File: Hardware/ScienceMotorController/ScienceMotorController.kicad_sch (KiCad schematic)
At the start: 200 parts

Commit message: Finished schematic and updated footprints
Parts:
- removed D? (x2): YELLOW, LED_SMD:LED_0603_1608Metric_Pad1.05x0.95mm_HandSolder, symbol Device:LED_Small
- removed LimSwitch? (x2): Molex_SL_02, MRDT_Connectors:MOLEX_SL_02_Vertical, symbol MRDT_Connectors:Molex_SL_02
- removed R? (x2): 120, Resistor_SMD:R_0603_1608Metric_Pad0.98x0.95mm_HandSolder, symbol Device:R
- removed Servo? (x2): Molex_SL_03, MRDT_Connectors:MOLEX_SL_03_Vertical, symbol MRDT_Connectors:Molex_SL_03
- added AbsEncode?: Molex_SL_03, MRDT_Connectors:MOLEX_SL_03_Vertical, symbol MRDT_Connectors:Molex_SL_03
- added Conn6: Molex_SL_02, MRDT_Connectors:MOLEX_SL_02_Vertical, symbol MRDT_Connectors:Molex_SL_02
- added D16: LED(B), LED_SMD:LED_0603_1608Metric_Pad1.05x0.95mm_HandSolder, symbol Device:LED
- added D?: YELLOW, LED_SMD:LED_0603_1608Metric_Pad1.05x0.95mm_HandSolder, symbol Device:LED_Small
- added Q10: AO3401A, Package_TO_SOT_SMD:SOT-23, symbol Transistor_FET:AO3401A
- added Q9: BSS138, Package_TO_SOT_SMD:SOT-23, symbol Transistor_FET:BSS138
- added R36: 4.7k, Resistor_SMD:R_0603_1608Metric_Pad0.98x0.95mm_HandSolder, symbol Device:R
- added R37, R38: 10k, Resistor_SMD:R_0603_1608Metric_Pad0.98x0.95mm_HandSolder, symbol Device:R
- added R39: 1k, Resistor_SMD:R_0603_1608Metric_Pad0.98x0.95mm_HandSolder, symbol Device:R
- added R?: 120, Resistor_SMD:R_0603_1608Metric_Pad0.98x0.95mm_HandSolder, symbol Device:R
- R1, R2, R34, R35, R40, R41, R54, R55: renamed from R?; footprint (none) -> Resistor_SMD:R_0603_1608Metric_Pad0.98x0.95mm_HandSolder
- gave numbers to parts that had none: 173
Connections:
- net +12V: now also Q10.2 (S), R37.1
- net +5V: now also AbsEncode?.3
- net Encoder_PWM_4: now also AbsEncode?.2, R?.1
- net FWD_PWM_4: now also U12.6 (OUT1D)
- net GND: now also AbsEncode?.1, Conn6.2, D16.1 (K), D?.1 (K), Q9.2 (S), R36.2
- net RVS_PWM_4: now also U12.7 (RX2)
- net Peristaltic Pump: now reaches U12.28 (RX7)
- net Peristaltic Pump: now also Q9.1 (G), R36.1
- new net: D16.2 (A), R39.1
- new net: Q9.3 (D), R38.2
- new net: Q10.1 (G), R37.2, R38.1
- new net: Conn6.1, Q10.3 (D), R39.2
- new net: D?.2 (A), R?.2
- no-connect marks 14 -> 13
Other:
- note added: "Motor Controllers"
- note removed: "Motor Drivers"
- moved on the sheet: AbsEncode1, AbsEncode2, AbsEncode3, AbsEncode4, C10, C11, C12, C7, C8, C9, Conn7A, Conn7B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

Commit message: Layout generated and organized. Still need to draw traces
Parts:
- added D33: YELLOW, LED_SMD:LED_0603_1608Metric_Pad1.05x0.95mm_HandSolder, symbol Device:LED_Small
- added DY13: LED, LED_SMD:LED_0603_1608Metric_Pad1.05x0.95mm_HandSolder, symbol Device:LED
- added LimSwitch3: Molex_SL_02, MRDT_Connectors:MOLEX_SL_02_Vertical, symbol MRDT_Connectors:Molex_SL_02
- added R58: 100, Resistor_SMD:R_0603_1608Metric_Pad0.98x0.95mm_HandSolder, symbol Device:R
- added R65: 120, Resistor_SMD:R_0603_1608Metric_Pad0.98x0.95mm_HandSolder, symbol Device:R
- added SW12: SW_Push, Button_Switch_SMD:SW_SPST_EVPBF, symbol Switch:SW_Push
- gave numbers to parts that had none: 3
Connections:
- net +3V3: now also LimSwitch3.1, SW12.1
- net GND: now also D33.1 (K), DY13.1 (K)
- net Limit_Switch_8: now also U12.30 (CRX3), LimSwitch3.2, R65.2
- net Motor_5_SW: now reaches U12.29 (TX7)
- net Motor_5_SW: now also R58.2, SW12.2
- new net: D33.2 (A), R65.1
- new net: DY13.2 (A), R58.1
- no-connect marks 13 -> 11

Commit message: More organization done
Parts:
- removed DY5, DY6: LED, LED_SMD:LED_0603_1608Metric_Pad1.05x0.95mm_HandSolder, symbol Device:LED
- removed R10, R9: 100, Resistor_SMD:R_0603_1608Metric_Pad0.98x0.95mm_HandSolder, symbol Device:R
- removed SW5, SW6: SW_Push, Button_Switch_SMD:SW_SPST_EVPBF, symbol Switch:SW_Push
- added C?: C, symbol Device:C
- U12: footprint MRDT_Shields:Teensy_4_1_Bare -> MRDT_Shields:Teensy_4_1_Ethernet
- renumbered LimSwitch7 to LimSwitch2, LimSwitch2 to LimSwitch3, LimSwitch8 to LimSwitch6, LimSwitch6 to LimSwitch7, LimSwitch3 to LimSwitch8, Servo6 to Servo1
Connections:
- net +12V: now also C?.1
- net Encoder_PWM_4: no longer AbsEncode5.2, R64.1
- net GND: now also C?.2
- net Limit_Switch_8: no longer U12.30 (CRX3)
- net Limit_Switch_9: no longer names the net of U12.39 (A15)
- net Servo_5 renamed Encoder_PWM_5
- net Encoder_PWM_5: now also AbsEncode5.2, R64.1
- net Servo_5_SW: no longer names the net of U12.31 (CTX3)
- net Servo_6: no longer names the net of U12.11 (MOSI)
- net Servo_6_SW: no longer names the net of U12.32 (OUT1B)
- no-connect marks 11 -> 16
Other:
- moved on the sheet: Conn1A, Conn1B, D5, R11

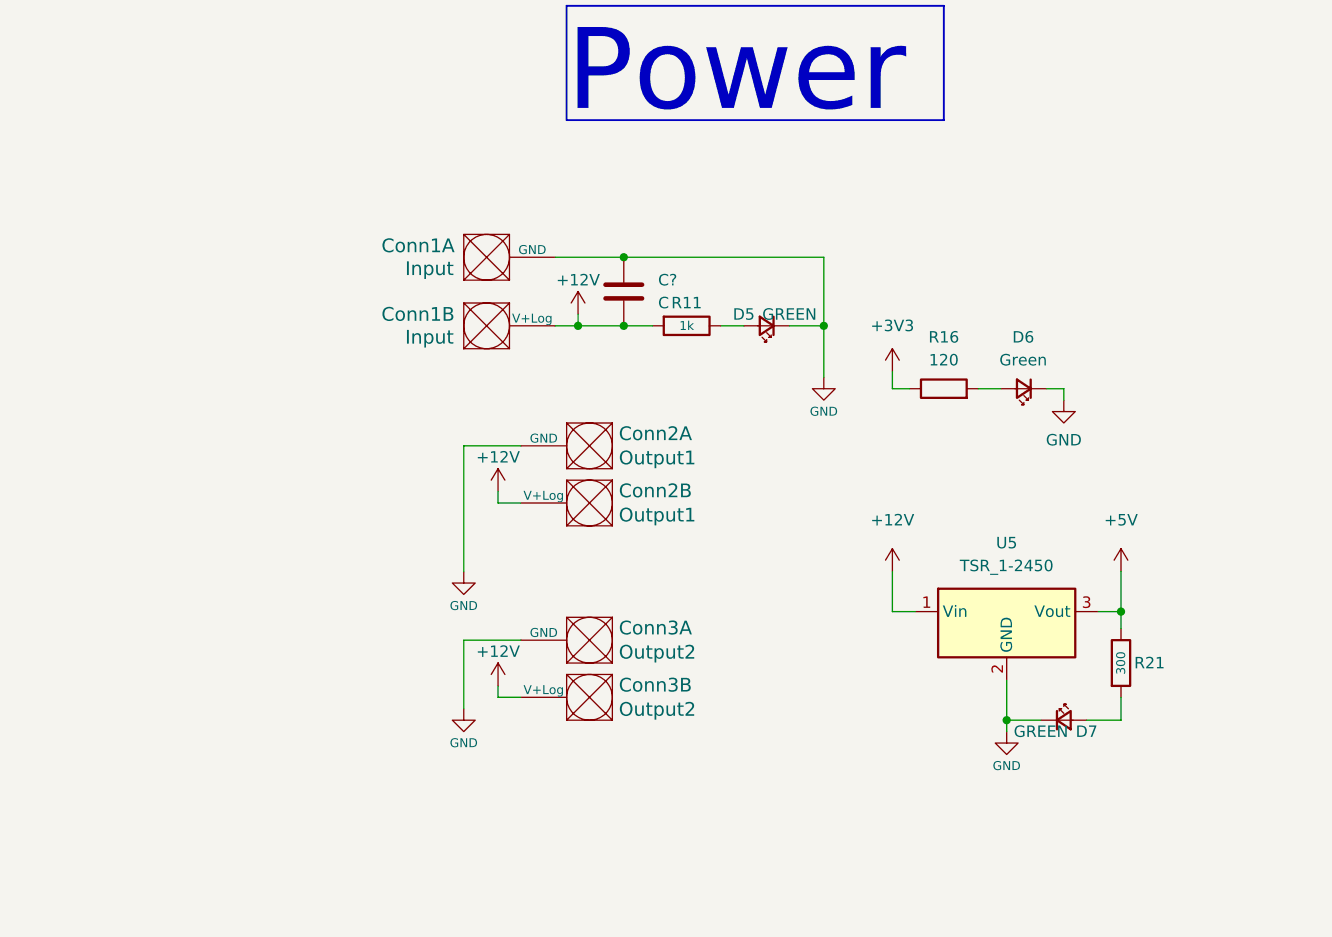
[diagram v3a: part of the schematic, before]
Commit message: H-Bridges made. Rough placement on board done
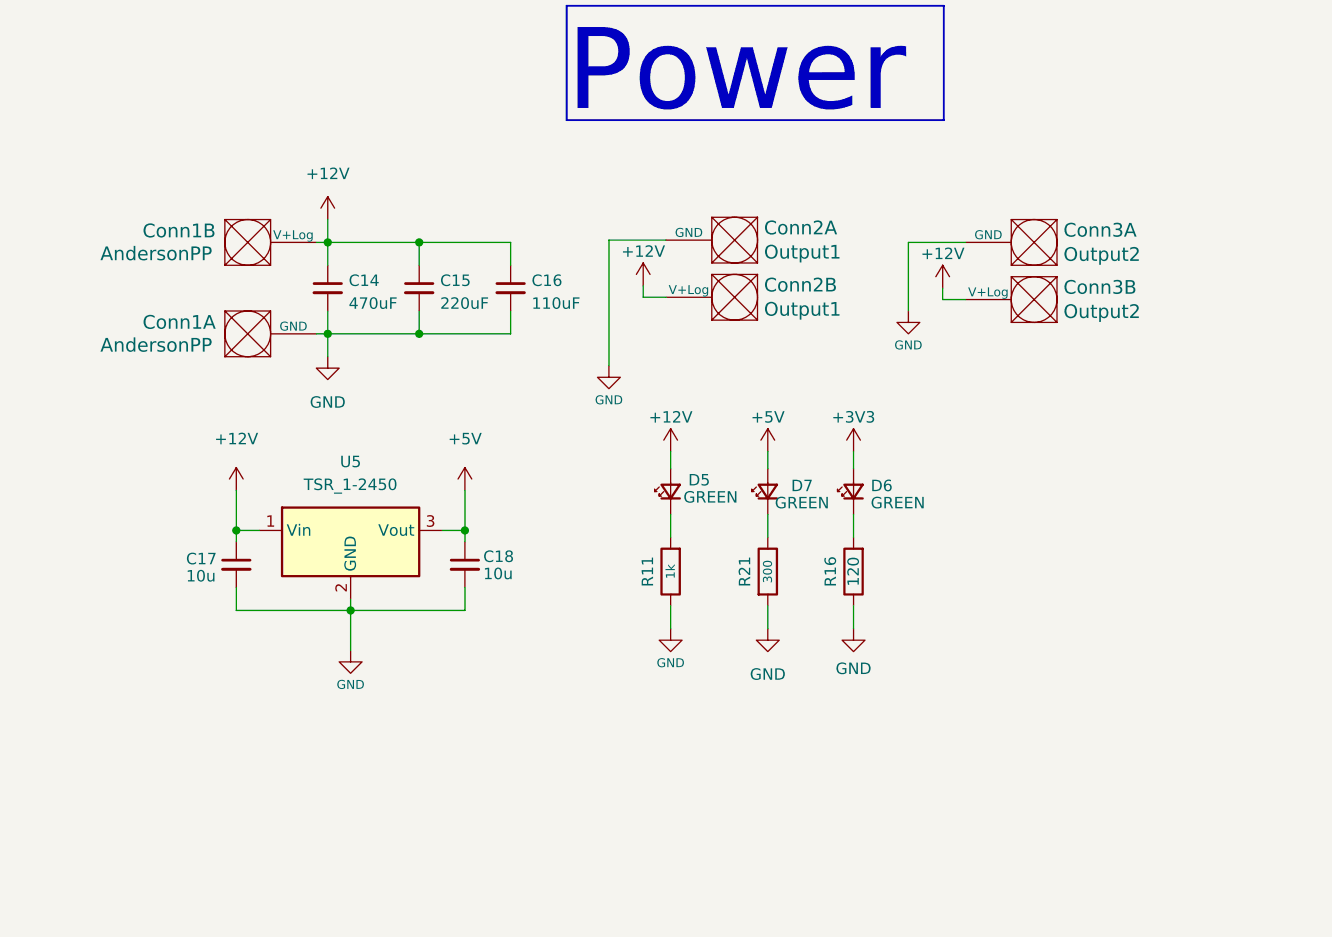
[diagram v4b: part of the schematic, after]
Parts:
- removed C?: C, symbol Device:C
- added C14: 470uF, Capacitor_THT:CP_Radial_D6.3mm_P2.50mm, symbol Device:C_Small
- added C15: 220uF, Capacitor_THT:CP_Radial_D6.3mm_P2.50mm, symbol Device:C_Small
- added C16: 110uF, Capacitor_THT:CP_Radial_D6.3mm_P2.50mm, symbol Device:C_Small
- added C17, C18: 10u, Capacitor_SMD:C_0603_1608Metric, symbol Device:C_Small
- Conn1: value Input -> AndersonPP
- D6: value Green -> GREEN
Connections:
- net +12V: now also D5.2 (A), C14.1, C15.1, C16.1, C17.1; no longer R11.2
- net +3V3: now also D6.2 (A); no longer R16.1
- net +5V: now also D7.2 (A), C18.1; no longer R21.1
- net GND: now also R11.1, R16.1, R21.2, C14.2, C15.2, C16.2, C17.2, C18.2; no longer D5.1 (K), D6.1 (K), D7.1 (K)
- net at R16.2: now also D6.1 (K); no longer D6.2 (A)
- new net: D7.1 (K), R21.1
- new net: D5.1 (K), R11.2
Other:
- moved on the sheet: Conn2A, Conn2B, Conn3A, Conn3B, D5, D6, D7, R11, R16, R21, U5

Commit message: H-Bridges traced internally
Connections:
- net FWD_PWM_5 is gone; now on net FWD_PWM_4: D17.2 (A), R40.1, U10.2 (HIN), U8.1
- net RVS_PWM_5 is gone; now on net RVS_PWM_4: D23.2 (A), R54.1, U13.2 (HIN), U8.3
- net Tx+: now reaches J1.1, U12.T+
- net Tx-: now reaches J1.3, U12.T (T-)
- net Rx+: now reaches J1.4, U12.R+
- net Rx-: now reaches J1.6, U12.R (R-)
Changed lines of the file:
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@@
+    (effects (font (size 1.27 1.27)) (justify left bottom))
+  )
+  (label "Tx-" (at 451.104 290.83 0)
     (effects (font (size 1.27 1.27)) (justify left bottom))
   )
@@
     (effects (font (size 1.27 1.27)) (justify left bottom))
   )
+  (label "Rx+" (at 450.85 298.45 0)
+    (effects (font (size 1.27 1.27)) (justify left bottom))
+  )
   (label "M4-" (at 401.955 109.855 0)
     (effects (font (size 1.27 1.27)) (justify left bottom))
   )
+  (label "Rx-" (at 450.85 295.91 0)
+    (effects (font (size 1.27 1.27)) (justify left bottom))
+  )
   (label "M4+" (at 111.76 57.15 0)
     (effects (font (size 1.27 1.27)) (justify left bottom))
   )
+  (label "Tx+" (at 451.104 293.37 0)
+    (effects (font (size 1.27 1.27)) (justify left bottom))
+  )
   (label "M4+" (at 358.14 59.69 0)
     (effects (font (size 1.27 1.27)) (justify left bottom))
@@
     )
   )
-  (global_label "RVS_PWM_5" (shape input) (at 485.14 100.965 0) (fields_autoplaced)
+  (global_label "RVS_PWM_4" (shape input) (at 485.14 100.965 0) (fields_autoplaced)
     (effects (font (size 1.27 1.27)) (justify left))
     (property "Intersheet References" "${INTERSHEET_REFS}" (id 0) (at 498.3499 100.8856 0)
@@
     )
   )
-  (global_label "FWD_PWM_5" (shape input) (at 281.94 100.965 180) (fields_autoplaced)
+  (global_label "FWD_PWM_4" (shape input) (at 281.94 100.965 180) (fields_autoplaced)
     (effects (font (size 1.27 1.27)) (justify right))
     (property "Intersheet References" "${INTERSHEET_REFS}" (id 0) (at 268.4882 100.8856 0)

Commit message: Traces done. Ground vias left
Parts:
- renumbered SW7 to SW5, SW8 to SW6, SW9 to SW7, SW10 to SW8, SW12 to SW9
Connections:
- net Encoder_PWM_1: now also U12.0 (RX1); no longer U12.14 (A0)
- net Encoder_PWM_2: now also U12.1 (TX1); no longer U12.15 (A1)
- net Encoder_PWM_3: now also U12.2 (OUT2); no longer U12.18 (A4)
- net Encoder_PWM_4: now also U12.3 (LRCLK2); no longer U12.19 (A5)
- net Encoder_PWM_5: now also U12.4 (BCLK2); no longer U12.12 (MISO)
- net FWD_PWM_1: now also U12.25 (A11); no longer U12.0 (RX1)
- net FWD_PWM_2: now also U12.10 (CS1); no longer U12.2 (OUT2)
- net FWD_PWM_3: now also U12.12 (MISO); no longer U12.4 (BCLK2)
- net FWD_PWM_4: now also U12.8 (TX2); no longer U12.6 (OUT1D)
- net GND: now also J1.SH
- net Limit_Switch_1: now also U12.40 (A16); no longer U12.23 (A9)
- net Limit_Switch_2: now also U12.39 (A15); no longer U12.22 (A8)
- net Limit_Switch_3: now also U12.38 (A14); no longer U12.21 (A7)
- net Limit_Switch_4: now also U12.37 (CS3); no longer U12.20 (A6)
- net Limit_Switch_5: now also U12.36 (CS2); no longer U12.17 (A3)
- net Limit_Switch_6: now also U12.35 (TX8); no longer U12.16 (A2)
- net Limit_Switch_7: now also U12.34 (RX8); no longer U12.41 (A17)
- net Limit_Switch_8: now also U12.33 (MCLK2); no longer U12.40 (A16)
- net Manual_Control_Left: now also U12.21 (A7); no longer U12.37 (CS3)
- net Manual_Control_Right: now also U12.20 (A6); no longer U12.38 (A14)
- net Motor_1_SW: now also U12.28 (RX7); no longer U12.27 (A13)
- net Motor_2_SW: now also U12.29 (TX7); no longer U12.26 (A12)
- net Motor_3_SW: now also U12.30 (CRX3); no longer U12.25 (A11)
- net Motor_4_SW: now also U12.31 (CTX3); no longer U12.24 (A10)
- net Motor_5_SW: now also U12.32 (OUT1B); no longer U12.29 (TX7)
- net Peristaltic Pump: now also U12.6 (OUT1D); no longer U12.28 (RX7)
- net RVS_PWM_1: now also U12.24 (A10); no longer U12.1 (TX1)
- net RVS_PWM_2: now also U12.9 (OUT1C); no longer U12.3 (LRCLK2)
- net RVS_PWM_3: now also U12.11 (MOSI); no longer U12.5 (IN2)
- net Servo_1: now also U12.19 (A5); no longer U12.8 (TX2)
- net Servo_1_SW: now also U12.15 (A1); no longer U12.36 (CS2)
- net Servo_2: now also U12.18 (A4); no longer U12.9 (OUT1C)
- net Servo_2_SW: now also U12.14 (A0); no longer U12.35 (TX8)
- net Servo_3: now also U12.22 (A8); no longer U12.10 (CS1)
- net Servo_3_SW: now also U12.13 (SCK); no longer U12.34 (RX8)
- net Servo_4: now also U12.23 (A9); no longer U12.13 (SCK)
- net Servo_4_SW: now also U12.41 (A17); no longer U12.33 (MCLK2)
- no-connect marks 16 -> 15
